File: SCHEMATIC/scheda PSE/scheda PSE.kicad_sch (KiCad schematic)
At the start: 0 parts

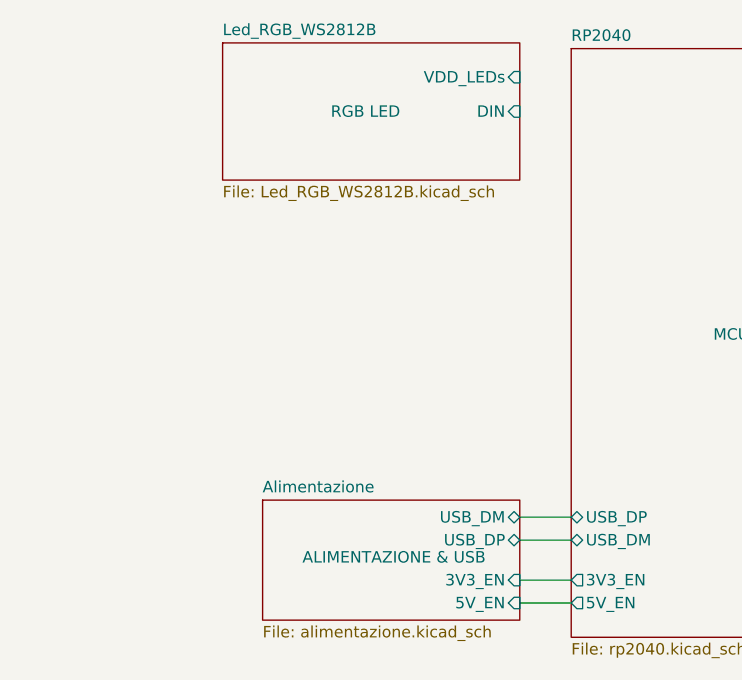
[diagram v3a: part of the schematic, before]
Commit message: aggiunta memoria EEPROM a schematico
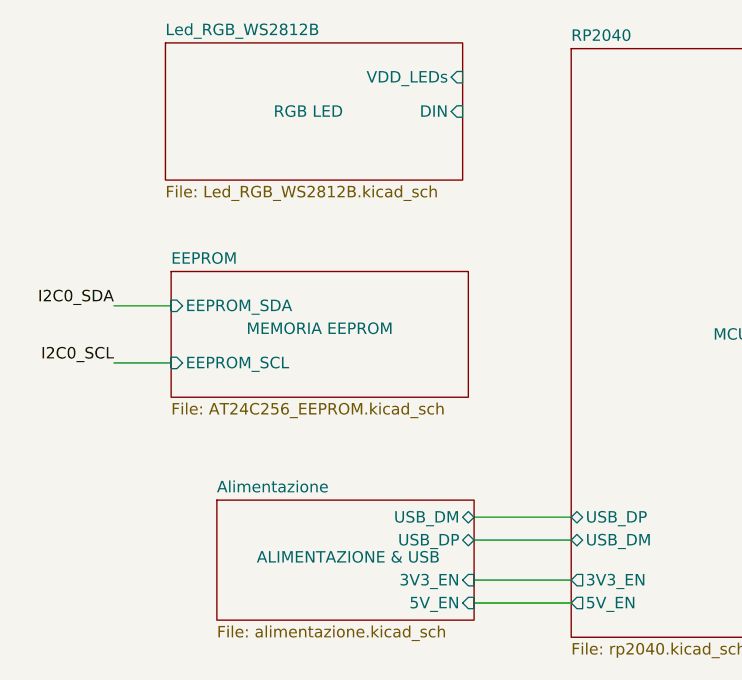
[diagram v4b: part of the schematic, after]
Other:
- added sheet EEPROM (AT24C256_EEPROM.kicad_sch)
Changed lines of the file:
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@@
     (stroke (width 0) (type default) (color 0 0 0 0))
   )
-  (wire (pts (xy 108.585 124.46) (xy 114.3 124.46))
+  (wire (pts (xy 103.505 124.46) (xy 114.3 124.46))
     (stroke (width 0) (type default) (color 0 0 0 0))
   )
@@
     (stroke (width 0) (type default) (color 0 0 0 0))
   )
-  (wire (pts (xy 108.585 117.475) (xy 114.3 117.475))
-    (stroke (width 0) (type default) (color 0 0 0 0))
-  )
-  (wire (pts (xy 108.585 127) (xy 114.3 127))
-    (stroke (width 0) (type default) (color 0 0 0 0))
-  )
-  (wire (pts (xy 108.585 120.015) (xy 114.3 120.015))
+  (wire (pts (xy 103.505 117.475) (xy 114.3 117.475))
+    (stroke (width 0) (type default) (color 0 0 0 0))
+  )
+  (wire (pts (xy 63.5 93.98) (xy 69.85 93.98))
+    (stroke (width 0) (type default) (color 0 0 0 0))
+  )
+  (wire (pts (xy 103.505 127) (xy 114.3 127))
+    (stroke (width 0) (type default) (color 0 0 0 0))
+  )
+  (wire (pts (xy 103.505 120.015) (xy 114.3 120.015))
+    (stroke (width 0) (type default) (color 0 0 0 0))
+  )
+  (wire (pts (xy 69.85 100.33) (xy 63.5 100.33))
     (stroke (width 0) (type default) (color 0 0 0 0))
   )
@@
     (effects (font (size 1.27 1.27)) (justify left bottom))
   )
+  (label "I2C0_SDA" (at 63.5 93.98 180)
+    (effects (font (size 1.27 1.27)) (justify right bottom))
+  )
   (label "I2C0_SCL" (at 207.01 87.63 180)
+    (effects (font (size 1.27 1.27)) (justify right bottom))
+  )
+  (label "I2C0_SCL" (at 63.5 100.33 180)
     (effects (font (size 1.27 1.27)) (justify right bottom))
   )
@@
     )
   )
-  (sheet (at 75.565 64.77) (size 33.02 15.24)
+  (sheet (at 69.215 64.77) (size 33.02 15.24)
     (stroke (width 0.1524) (type solid) (color 0 0 0 0))
     (fill (color 0 0 0 0.0000))
-    (property "Sheet name" "Led_RGB_WS2812B" (id 0) (at 75.565 64.0584 0)
+    (property "Sheet name" "Led_RGB_WS2812B" (id 0) (at 69.215 64.0584 0)
       (effects (font (size 1.27 1.27)) (justify left bottom))
     )
-    (property "Sheet file" "Led_RGB_WS2812B.kicad_sch" (id 1) (at 75.565 80.5946 0)
+    (property "Sheet file" "Led_RGB_WS2812B.kicad_sch" (id 1) (at 69.215 80.5946 0)
       (effects (font (size 1.27 1.27)) (justify left top))
     )
-    (property "Etichetta" "RGB LED" (id 2) (at 91.44 72.39 0))
-    (pin "VDD_LEDs" input (at 108.585 68.58 0)
-      (effects (font (size 1.27 1.27)) (justify right))
-    )
-    (pin "DIN" input (at 108.585 72.39 0)
+    (property "Etichetta" "RGB LED" (id 2) (at 85.09 72.39 0))
+    (pin "VDD_LEDs" input (at 102.235 68.58 0)
+      (effects (font (size 1.27 1.27)) (justify right))
+    )
+    (pin "DIN" input (at 102.235 72.39 0)
       (effects (font (size 1.27 1.27)) (justify right))
     )
@@
     )
   )
-  (sheet (at 80.01 115.57) (size 28.575 13.335)
+  (sheet (at 74.93 115.57) (size 28.575 13.335)
     (stroke (width 0.1524) (type solid) (color 0 0 0 0))
     (fill (color 0 0 0 0.0000))
-    (property "Sheet name" "Alimentazione" (id 0) (at 80.01 114.8584 0)
+    (property "Sheet name" "Alimentazione" (id 0) (at 74.93 114.8584 0)
       (effects (font (size 1.27 1.27)) (justify left bottom))
     )
-    (property "Sheet file" "alimentazione.kicad_sch" (id 1) (at 80.01 129.4896 0)
+    (property "Sheet file" "alimentazione.kicad_sch" (id 1) (at 74.93 129.4896 0)
       (effects (font (size 1.27 1.27)) (justify left top))
     )
-    (property "Etichetta" "ALIMENTAZIONE & USB" (id 2) (at 94.615 121.92 0))
-    (pin "USB_DP" bidirectional (at 108.585 120.015 0)
-      (effects (font (size 1.27 1.27)) (justify right))
-    )
-    (pin "USB_DM" bidirectional (at 108.585 117.475 0)
-      (effects (font (size 1.27 1.27)) (justify right))
-    )
-    (pin "3V3_EN" input (at 108.585 124.46 0)
-      (effects (font (size 1.27 1.27)) (justify right))
-    )
-    (pin "5V_EN" input (at 108.585 127 0)
+    (property "Etichetta" "ALIMENTAZIONE & USB" (id 2) (at 89.535 121.92 0))
+    (pin "USB_DP" bidirectional (at 103.505 120.015 0)
+      (effects (font (size 1.27 1.27)) (justify right))
+    )
+    (pin "USB_DM" bidirectional (at 103.505 117.475 0)
+      (effects (font (size 1.27 1.27)) (justify right))
+    )
+    (pin "3V3_EN" input (at 103.505 124.46 0)
+      (effects (font (size 1.27 1.27)) (justify right))
+    )
+    (pin "5V_EN" input (at 103.505 127 0)
       (effects (font (size 1.27 1.27)) (justify right))
     )
@@
     (pin "LED_ALIVE" output (at 149.86 129.54 0)
       (effects (font (size 1.27 1.27)) (justify right))
+    )
+  )
+  (sheet (at 69.85 90.17) (size 33.02 13.97)
+    (stroke (width 0.1524) (type solid) (color 0 0 0 0))
+    (fill (color 0 0 0 0.0000))
+    (property "Sheet name" "EEPROM" (id 0) (at 69.85 89.4584 0)
+      (effects (font (size 1.27 1.27)) (justify left bottom))
+    )
+    (property "Sheet file" "AT24C256_EEPROM.kicad_sch" (id 1) (at 69.85 104.7246 0)
+      (effects (font (size 1.27 1.27)) (justify left top))
+    )
+    (property "Etichetta" "MEMORIA EEPROM" (id 2) (at 86.36 96.52 0))
+    (pin "EEPROM_SDA" input (at 69.85 93.98 180)
+      (effects (font (size 1.27 1.27)) (justify left))
+    )
+    (pin "EEPROM_SCL" input (at 69.85 100.33 180)
+      (effects (font (size 1.27 1.27)) (justify left))
     )
   )
@@
     (path "/7ee2252d-ff7a-4cf9-a8b8-589518dbae10" (page "6"))
     (path "/7389e30f-cc4a-4964-bca3-cd95052ca62a" (page "6"))
+    (path "/e11985b0-9a1c-439c-a505-c624f651adb8" (page "7"))
   )
   (symbol_instances
@@
       (reference "#PWR?") (unit 1) (value "GNDA") (footprint "")
     )
+    (path "/e11985b0-9a1c-439c-a505-c624f651adb8/4cc695d1-7446-4ed9-8387-60a1df35443e"
+      (reference "#PWR?") (unit 1) (value "+3.3V") (footprint "")
+    )
     (path "/9f40c713-1bcb-4f1c-9e01-30533e77b65d/4cdc0c3e-ba82-41b5-9d62-25412e08be35"
       (reference "#PWR?") (unit 1) (value "GND") (footprint "")
@@
       (reference "#PWR?") (unit 1) (value "+5V") (footprint "")
     )
+    (path "/e11985b0-9a1c-439c-a505-c624f651adb8/6b47f5fa-64e7-400e-b074-98103a97a685"
+      (reference "#PWR?") (unit 1) (value "GND") (footprint "")
+    )
     (path "/7ee2252d-ff7a-4cf9-a8b8-589518dbae10/6bd3f247-c0b6-4aa3-af29-9067a8b346d1"
       (reference "#PWR?") (unit 1) (value "GND") (footprint "")
@@
       (reference "#PWR?") (unit 1) (value "GND") (footprint "")
     )
+    (path "/e11985b0-9a1c-439c-a505-c624f651adb8/fffdc1ec-6ac5-41a4-8064-9dc1bbd7af98"
+      (reference "#PWR?") (unit 1) (value "GND") (footprint "")
+    )
     (path "/79aec321-3c99-4e59-b384-4589f6950bd0/843d4752-6e63-4d95-a426-482380d37ea8"
       (reference "BZ?") (unit 1) (value "Buzzer") (footprint "Buzzer_Beeper:MagneticBuzzer_Kingstate_KCG0601")
@@
       (reference "U?") (unit 1) (value "XC6705A331MR-G") (footprint "Package_TO_SOT_SMD:SOT-23-5")
     )
+    (path "/e11985b0-9a1c-439c-a505-c624f651adb8/2f322348-3a99-480f-b1e6-01d64a21c9b3"
+      (reference "U?") (unit 1) (value "AT24C256") (footprint "")
+    )
     (path "/79aec321-3c99-4e59-b384-4589f6950bd0/3168c647-03a8-4d4f-86e8-5e4e0f83c41f"

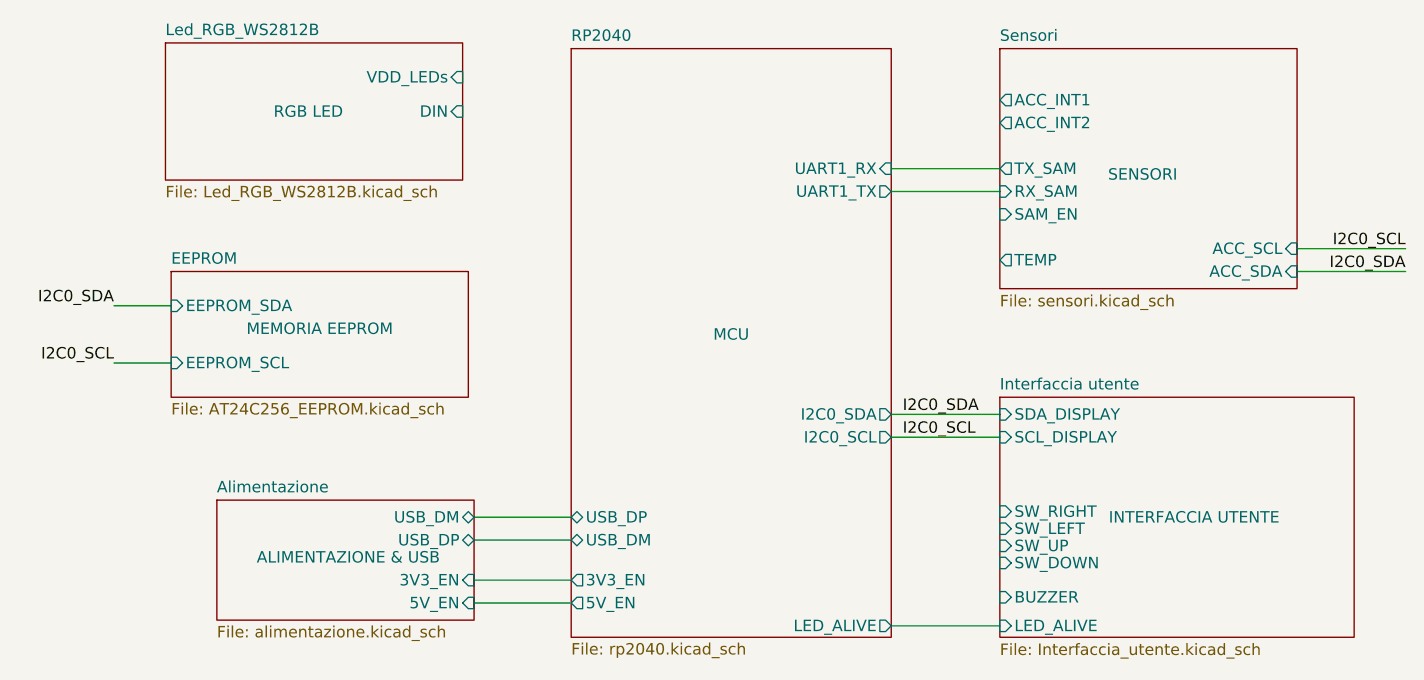
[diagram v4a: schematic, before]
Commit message: sistemato tutto, e aggiunti i footprint da modificare
sistemato tutto, aggiunto e modificato i footprint.
Manca solo aggiungere i restanti footprint (praticamente solo dei componenti comuni)
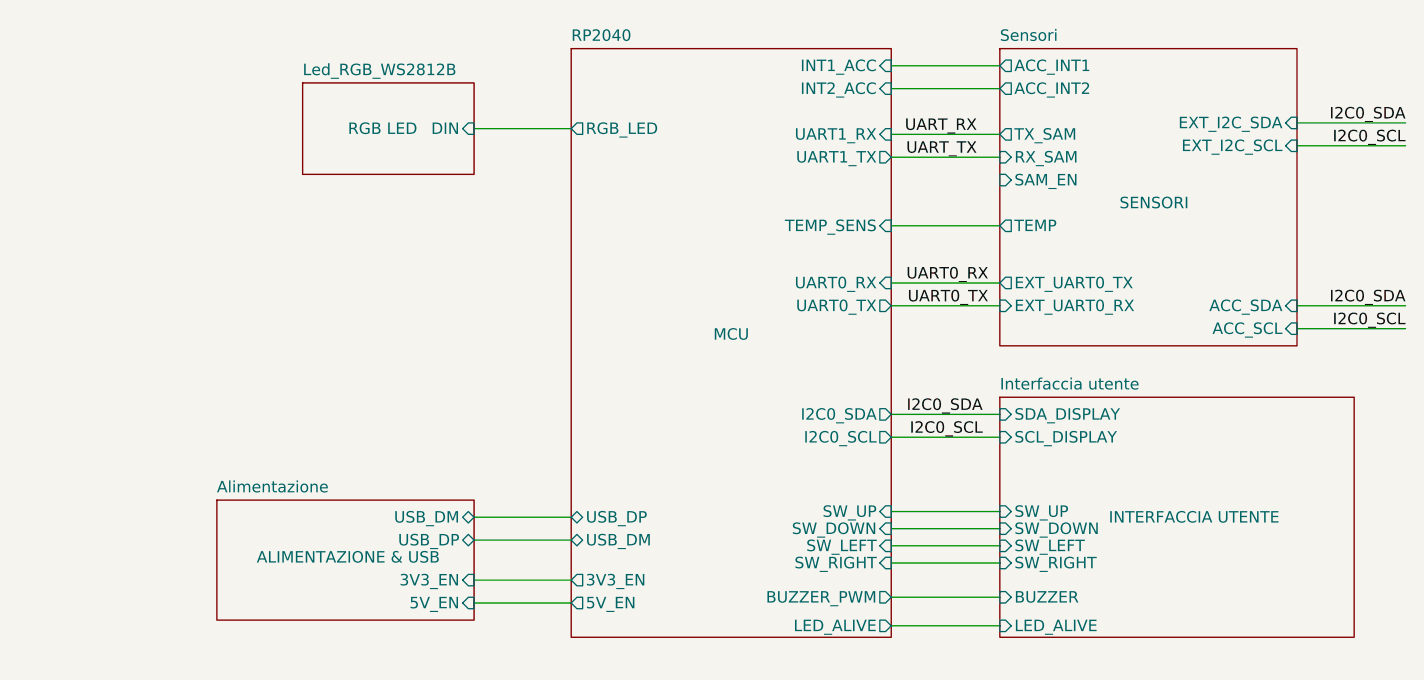
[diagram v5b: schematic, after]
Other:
- removed sheet EEPROM
- sheet Led_RGB_WS2812B ports: added none; removed VDD_LEDs
- sheet RP2040 ports: added BUZZER_PWM, INT1_ACC, INT2_ACC, RGB_LED, SW_DOWN, SW_LEFT, SW_RIGHT, SW_UP, TEMP_SENS, UART0_RX, UART0_TX; removed none
- sheet Sensori ports: added EXT_I2C_SCL, EXT_I2C_SDA, EXT_UART0_RX, EXT_UART0_TX; removed none

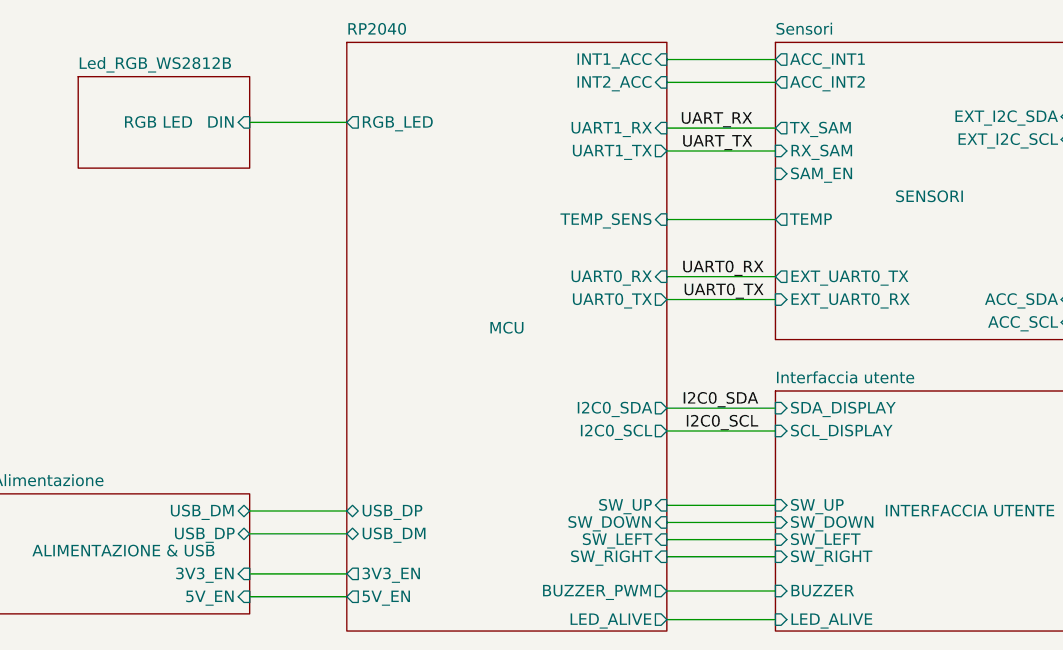
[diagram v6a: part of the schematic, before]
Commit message: Aggiunti QUASI tutti i footprint
aggiunti quasi tutti i footprint dei componenti
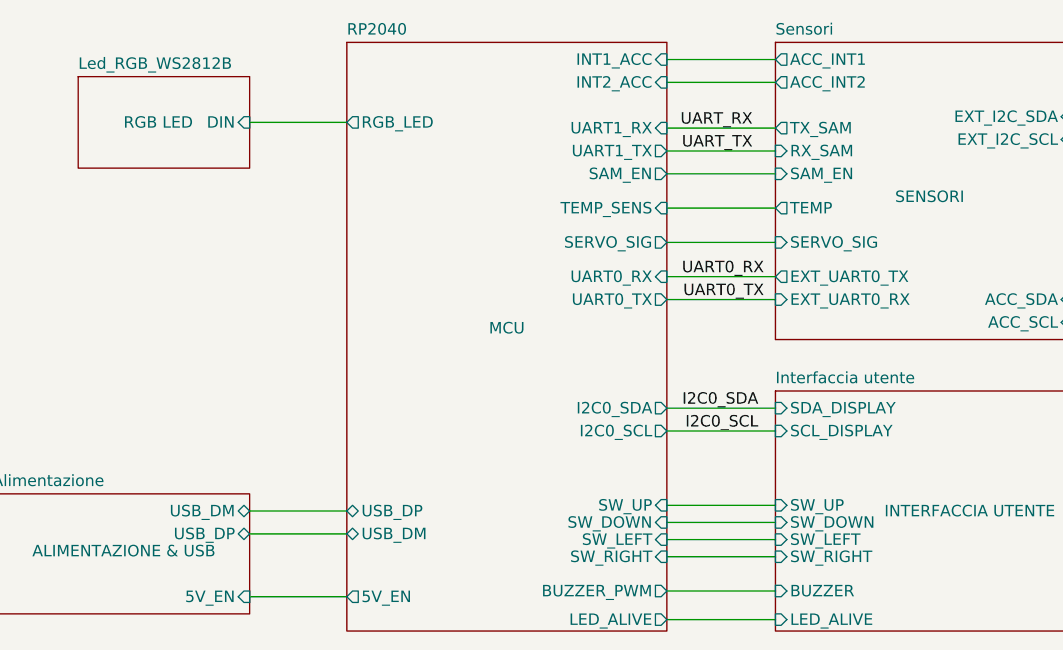
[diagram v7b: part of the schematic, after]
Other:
- sheet Alimentazione ports: added none; removed 3V3_EN
- sheet RP2040 ports: added SAM_EN, SERVO_SIG; removed 3V3_EN
- sheet Sensori ports: added SERVO_SIG; removed none

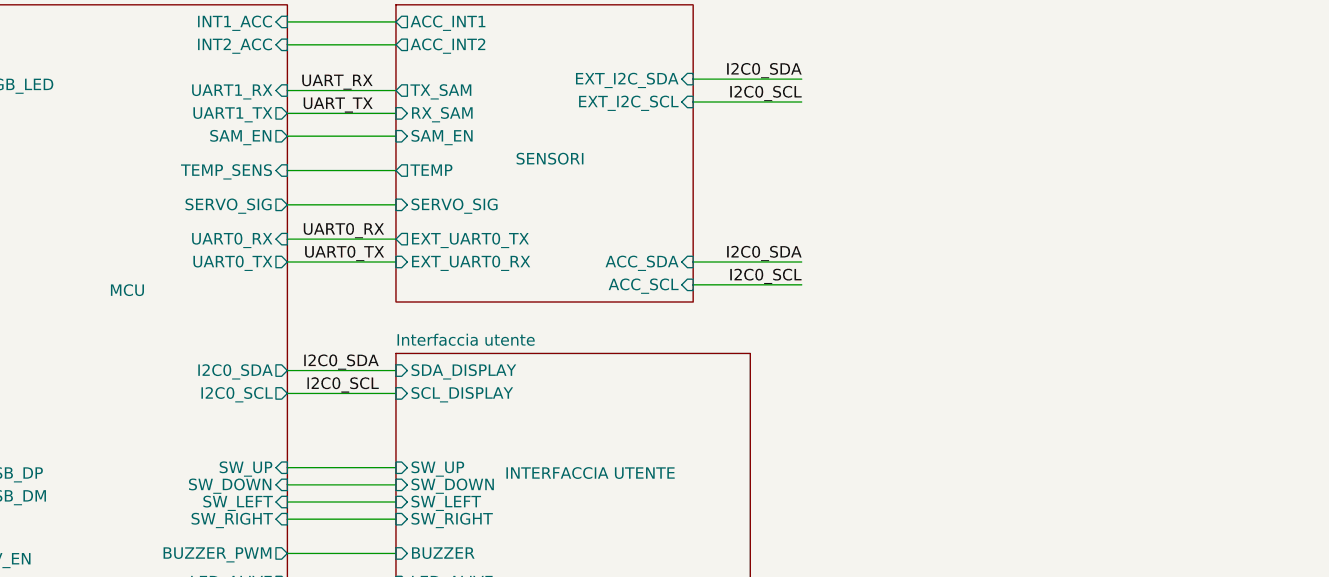
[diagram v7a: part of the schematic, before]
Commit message: iniziato il layout, posizionati componenti principali
incominciato il posizionamento dei componenti nel layout. Sono stati posizionati i componenti principali come led RGB, GPS, schermo, pulsanti vari, buzzer
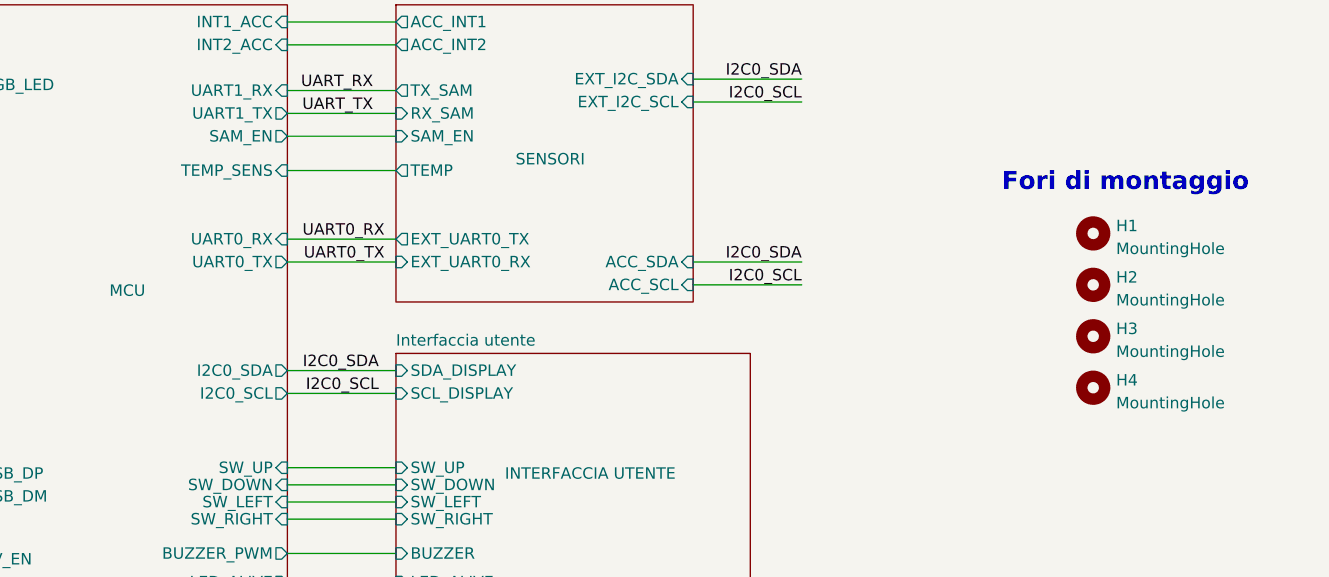
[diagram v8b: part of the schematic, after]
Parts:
- added H1, H2, H3, H4: MountingHole, MountingHole:MountingHole_3.2mm_M3_Pad_Via, symbol Mechanical:MountingHole
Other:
- sheet RP2040 ports: added none; removed SERVO_SIG
- sheet Sensori ports: added none; removed SERVO_SIG
- note added: "Fori di montaggio"
